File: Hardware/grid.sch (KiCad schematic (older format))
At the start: 269 parts, among them Q1 BSH205G2, Q10 BSH205G2, Q11 BSH205G2, Q12 BSH205G2, Q13 BSH205G2, Q14 BSH205G2, Q15 BSH205G2, Q16 BSH205G2, Q17 BSH205G2, Q18 BSH205G2, Q19 BSH205G2, Q2 BSH205G2, Q20 BSH205G2, Q21 NX7002AK, Q22 NX7002AK, Q23 NX7002AK, Q24 NX7002AK, Q25 NX7002AK, Q26 NX7002AK, Q27 NX7002AK, Q28 NX7002AK, Q29 NX7002AK, Q3 BSH205G2, Q30 NX7002AK, Q31 NX7002AK, Q32 NX7002AK, Q4 BSH205G2, Q5 BSH205G2, Q6 BSH205G2, Q7 BSH205G2, Q8 BSH205G2, Q9 BSH205G2, SW1 Button_matrix_4x4, SW10 SW_Push, SW11 SW_Push, SW12 SW_Push, SW13 SW_Push, SW14 SW_Push, SW15 SW_Push, SW16 SW_Push, SW17 SW_Push, SW18 SW_Push, SW19 SW_Push, SW2 Button_matrix_4x4, SW20 SW_Push, SW3 Button_matrix_4x4, SW4 Button_matrix_4x4, SW5 SW_Push, SW6 SW_Push, SW7 SW_Push, SW8 SW_Push, SW9 SW_Push, U2 74HC138, U3 74HC138, U4 74HC138

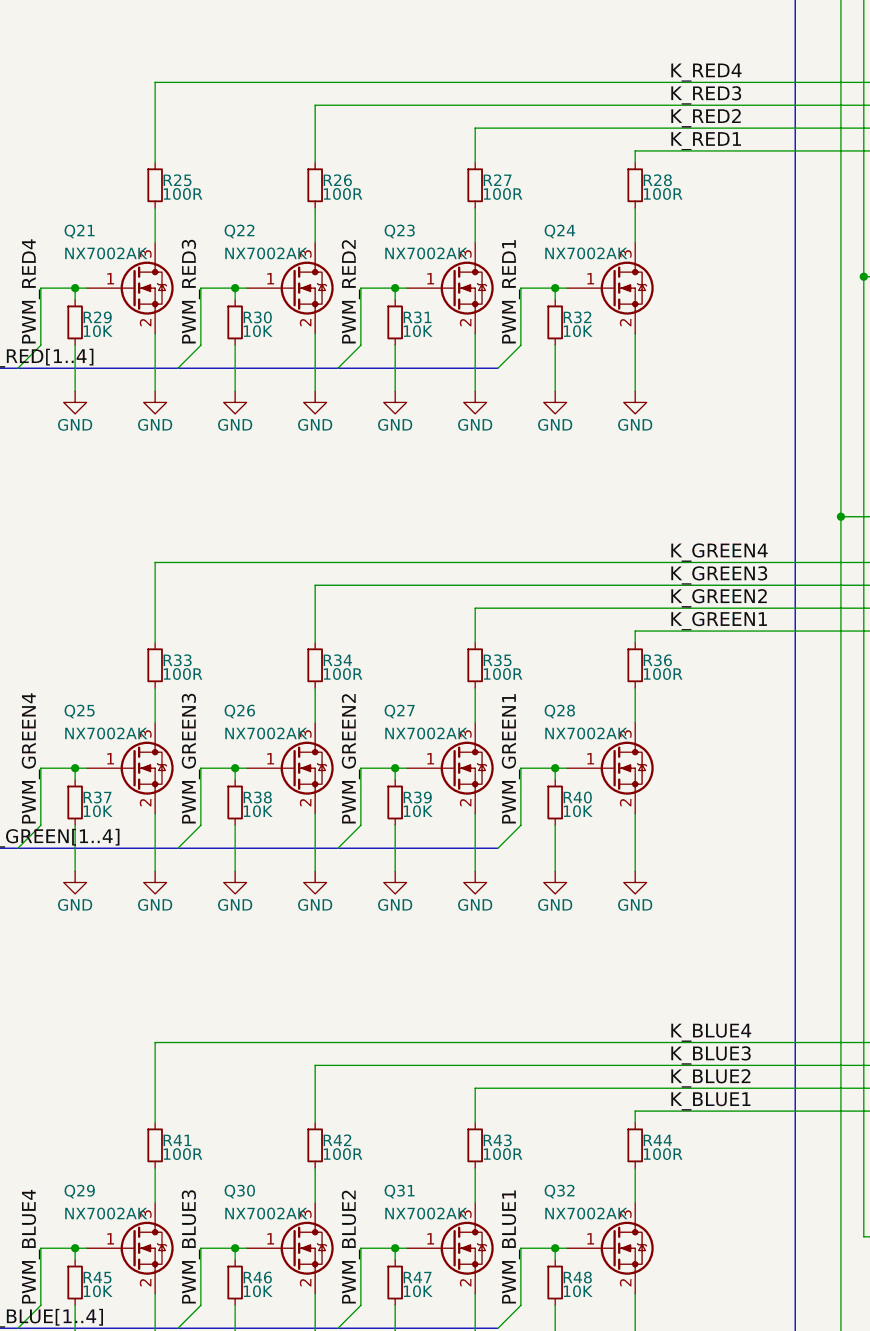
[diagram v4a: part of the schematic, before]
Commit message: changed LED current limiting resistor values
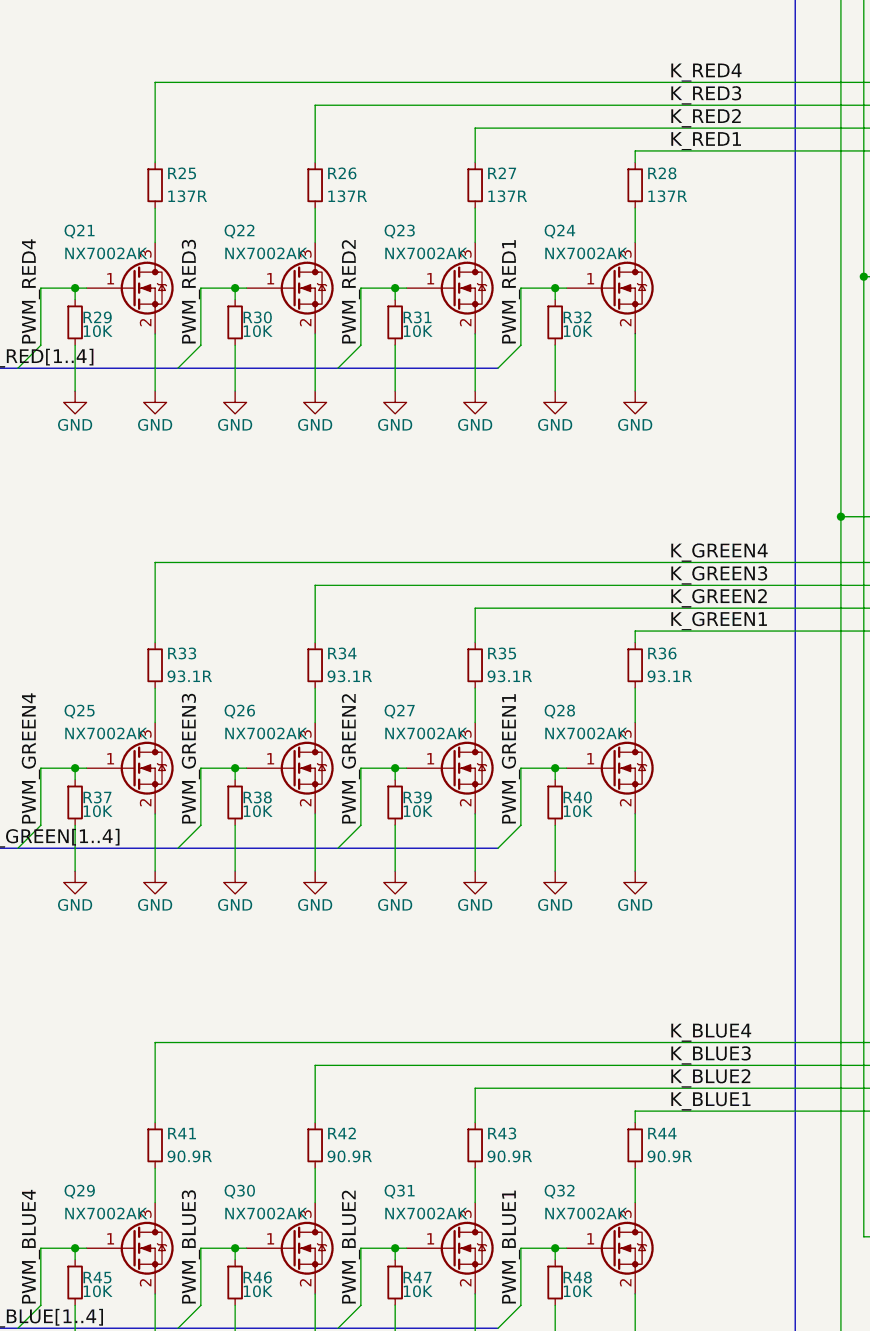
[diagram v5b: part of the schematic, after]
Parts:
- R25, R26, R27, R28: value 100R -> 137R
- R33, R34, R35, R36: value 100R -> 93.1R
- R41, R42, R43, R44: value 100R -> 90.9R
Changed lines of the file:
@@
 U 1 1 5A4E3C59
 P 4850 5800
-F 0 "R28" H 4880 5820 50  0000 L CNN
-F 1 "100R" H 4880 5760 50  0000 L CNN
+F 0 "R28" H 4900 5850 50  0000 L CNN
+F 1 "137R" H 4900 5750 50  0000 L CNN
 F 2 "project_library:R_1206" H 4850 5800 50  0001 C CNN
 F 3 "" H 4850 5800 50  0001 C CNN
@@
 U 1 1 5A4E72E9
 P 4150 5800
-F 0 "R27" H 4180 5820 50  0000 L CNN
-F 1 "100R" H 4180 5760 50  0000 L CNN
+F 0 "R27" H 4200 5850 50  0000 L CNN
+F 1 "137R" H 4200 5750 50  0000 L CNN
 F 2 "project_library:R_1206" H 4150 5800 50  0001 C CNN
 F 3 "" H 4150 5800 50  0001 C CNN
@@
 U 1 1 5A4E76B2
 P 3450 5800
-F 0 "R26" H 3480 5820 50  0000 L CNN
-F 1 "100R" H 3480 5760 50  0000 L CNN
+F 0 "R26" H 3500 5850 50  0000 L CNN
+F 1 "137R" H 3500 5750 50  0000 L CNN
 F 2 "project_library:R_1206" H 3450 5800 50  0001 C CNN
 F 3 "" H 3450 5800 50  0001 C CNN
@@
 U 1 1 5A4E7A7C
 P 2750 5800
-F 0 "R25" H 2780 5820 50  0000 L CNN
-F 1 "100R" H 2780 5760 50  0000 L CNN
+F 0 "R25" H 2800 5850 50  0000 L CNN
+F 1 "137R" H 2800 5750 50  0000 L CNN
 F 2 "project_library:R_1206" H 2750 5800 50  0001 C CNN
 F 3 "" H 2750 5800 50  0001 C CNN
@@
 U 1 1 5A4F1565
 P 4850 10000
-F 0 "R44" H 4880 10020 50  0000 L CNN
-F 1 "100R" H 4880 9960 50  0000 L CNN
+F 0 "R44" H 4900 10050 50  0000 L CNN
+F 1 "90.9R" H 4900 9950 50  0000 L CNN
 F 2 "project_library:R_1206" H 4850 10000 50  0001 C CNN
 F 3 "" H 4850 10000 50  0001 C CNN
@@
 U 1 1 5A4F156B
 P 4150 10000
-F 0 "R43" H 4180 10020 50  0000 L CNN
-F 1 "100R" H 4180 9960 50  0000 L CNN
+F 0 "R43" H 4200 10050 50  0000 L CNN
+F 1 "90.9R" H 4200 9950 50  0000 L CNN
 F 2 "project_library:R_1206" H 4150 10000 50  0001 C CNN
 F 3 "" H 4150 10000 50  0001 C CNN
@@
 U 1 1 5A4F1571
 P 3450 10000
-F 0 "R42" H 3480 10020 50  0000 L CNN
-F 1 "100R" H 3480 9960 50  0000 L CNN
+F 0 "R42" H 3500 10050 50  0000 L CNN
+F 1 "90.9R" H 3500 9950 50  0000 L CNN
 F 2 "project_library:R_1206" H 3450 10000 50  0001 C CNN
 F 3 "" H 3450 10000 50  0001 C CNN
@@
 U 1 1 5A4F1577
 P 2750 10000
-F 0 "R41" H 2780 10020 50  0000 L CNN
-F 1 "100R" H 2780 9960 50  0000 L CNN
+F 0 "R41" H 2800 10050 50  0000 L CNN
+F 1 "90.9R" H 2800 9950 50  0000 L CNN
 F 2 "project_library:R_1206" H 2750 10000 50  0001 C CNN
 F 3 "" H 2750 10000 50  0001 C CNN
@@
 U 1 1 5A4FC77F
 P 4850 7900
-F 0 "R36" H 4880 7920 50  0000 L CNN
-F 1 "100R" H 4880 7860 50  0000 L CNN
+F 0 "R36" H 4900 7950 50  0000 L CNN
+F 1 "93.1R" H 4900 7850 50  0000 L CNN
 F 2 "project_library:R_1206" H 4850 7900 50  0001 C CNN
 F 3 "" H 4850 7900 50  0001 C CNN
@@
 U 1 1 5A4FC785
 P 4150 7900
-F 0 "R35" H 4180 7920 50  0000 L CNN
-F 1 "100R" H 4180 7860 50  0000 L CNN
+F 0 "R35" H 4200 7950 50  0000 L CNN
+F 1 "93.1R" H 4200 7850 50  0000 L CNN
 F 2 "project_library:R_1206" H 4150 7900 50  0001 C CNN
 F 3 "" H 4150 7900 50  0001 C CNN
@@
 U 1 1 5A4FC78B
 P 3450 7900
-F 0 "R34" H 3480 7920 50  0000 L CNN
-F 1 "100R" H 3480 7860 50  0000 L CNN
+F 0 "R34" H 3500 7950 50  0000 L CNN
+F 1 "93.1R" H 3500 7850 50  0000 L CNN
 F 2 "project_library:R_1206" H 3450 7900 50  0001 C CNN
 F 3 "" H 3450 7900 50  0001 C CNN
@@
 U 1 1 5A4FC791
 P 2750 7900
-F 0 "R33" H 2780 7920 50  0000 L CNN
-F 1 "100R" H 2780 7860 50  0000 L CNN
+F 0 "R33" H 2800 7950 50  0000 L CNN
+F 1 "93.1R" H 2800 7850 50  0000 L CNN
 F 2 "project_library:R_1206" H 2750 7900 50  0001 C CNN
 F 3 "" H 2750 7900 50  0001 C CNN

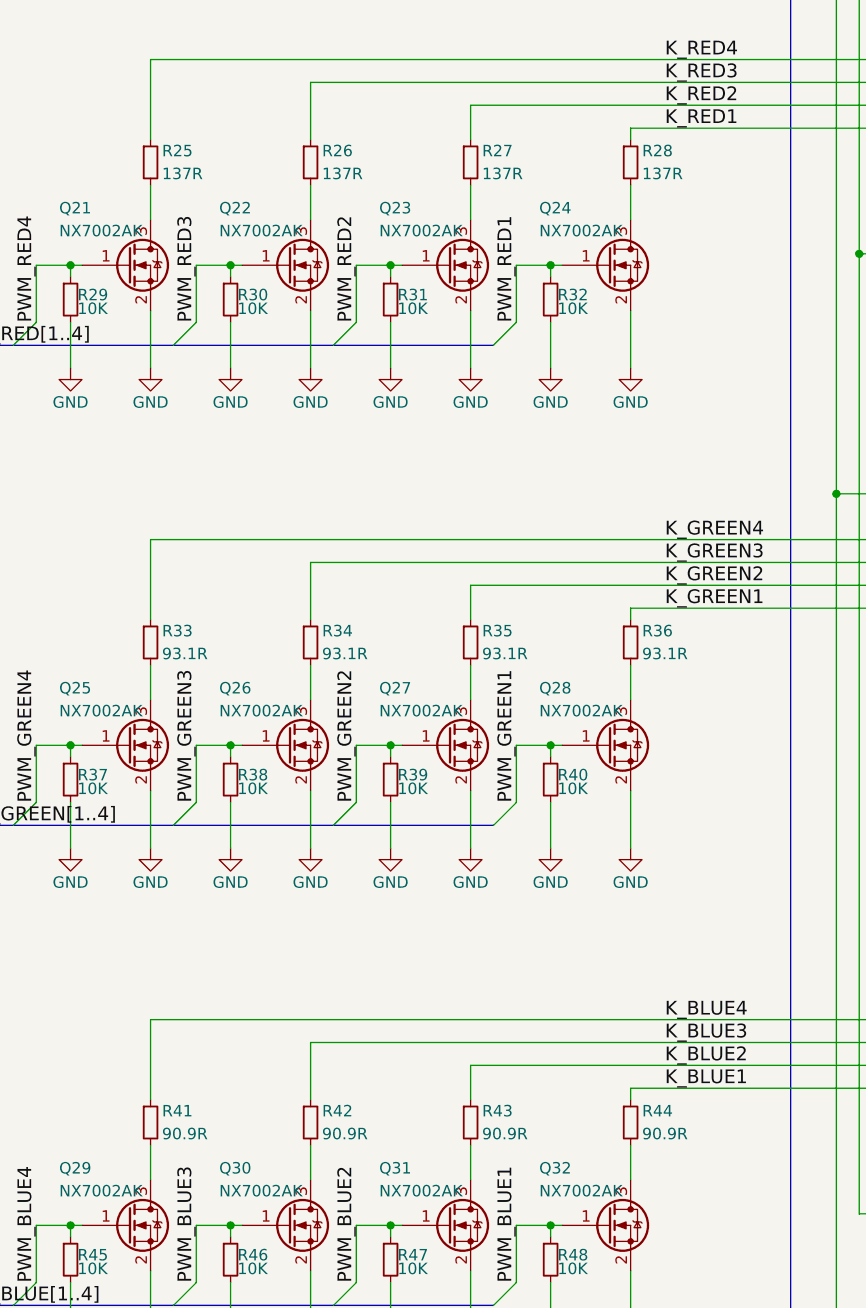
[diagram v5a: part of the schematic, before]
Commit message: changed resistor values, added drum layout output
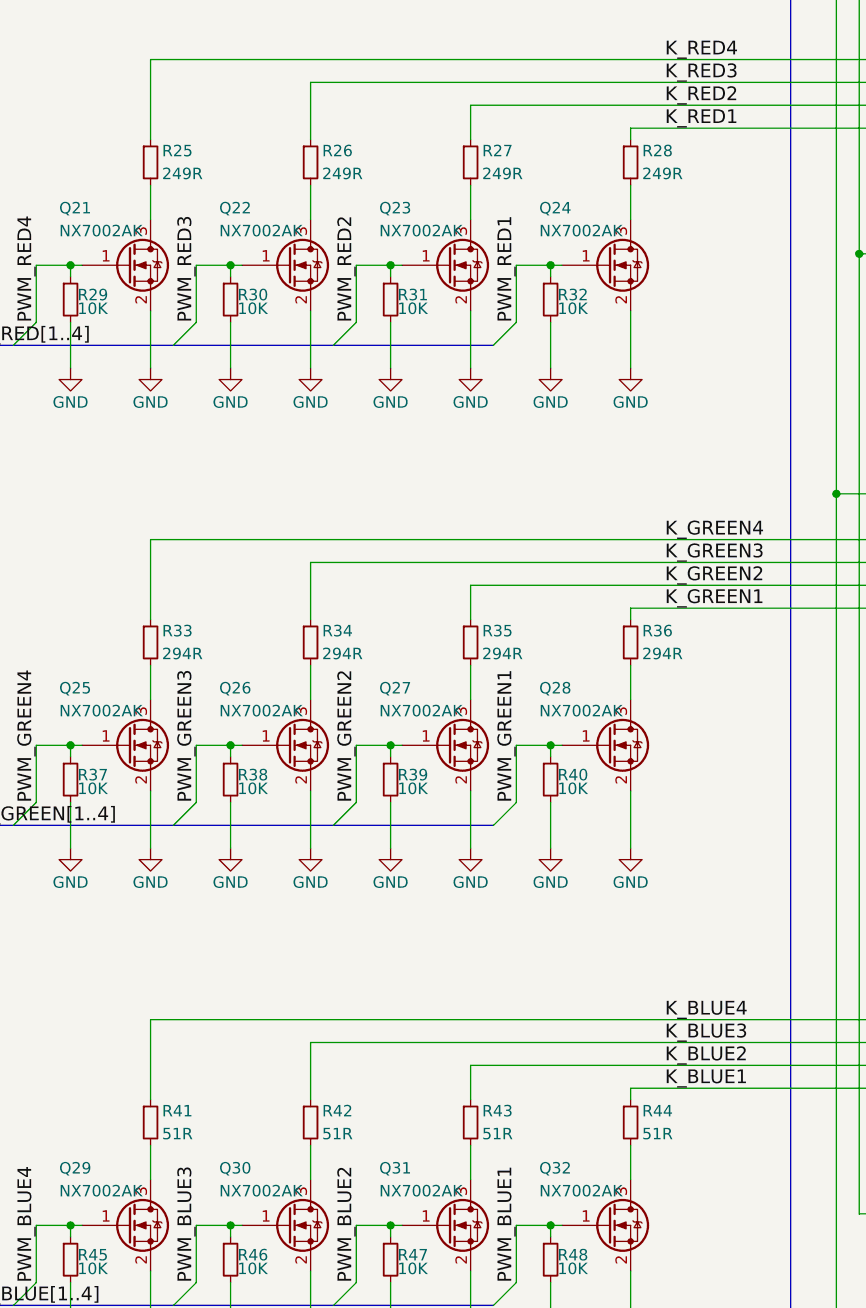
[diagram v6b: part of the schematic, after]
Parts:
- R25, R26, R27, R28: value 137R -> 249R
- R33, R34, R35, R36: value 93.1R -> 294R
- R41, R42, R43, R44: value 90.9R -> 51R
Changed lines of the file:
@@
 P 4850 5800
 F 0 "R28" H 4900 5850 50  0000 L CNN
-F 1 "137R" H 4900 5750 50  0000 L CNN
+F 1 "249R" H 4900 5750 50  0000 L CNN
 F 2 "project_library:R_1206" H 4850 5800 50  0001 C CNN
 F 3 "" H 4850 5800 50  0001 C CNN
@@
 P 4150 5800
 F 0 "R27" H 4200 5850 50  0000 L CNN
-F 1 "137R" H 4200 5750 50  0000 L CNN
+F 1 "249R" H 4200 5750 50  0000 L CNN
 F 2 "project_library:R_1206" H 4150 5800 50  0001 C CNN
 F 3 "" H 4150 5800 50  0001 C CNN
@@
 P 3450 5800
 F 0 "R26" H 3500 5850 50  0000 L CNN
-F 1 "137R" H 3500 5750 50  0000 L CNN
+F 1 "249R" H 3500 5750 50  0000 L CNN
 F 2 "project_library:R_1206" H 3450 5800 50  0001 C CNN
 F 3 "" H 3450 5800 50  0001 C CNN
@@
 P 2750 5800
 F 0 "R25" H 2800 5850 50  0000 L CNN
-F 1 "137R" H 2800 5750 50  0000 L CNN
+F 1 "249R" H 2800 5750 50  0000 L CNN
 F 2 "project_library:R_1206" H 2750 5800 50  0001 C CNN
 F 3 "" H 2750 5800 50  0001 C CNN
@@
 P 4850 10000
 F 0 "R44" H 4900 10050 50  0000 L CNN
-F 1 "90.9R" H 4900 9950 50  0000 L CNN
+F 1 "51R" H 4900 9950 50  0000 L CNN
 F 2 "project_library:R_1206" H 4850 10000 50  0001 C CNN
 F 3 "" H 4850 10000 50  0001 C CNN
@@
 P 4150 10000
 F 0 "R43" H 4200 10050 50  0000 L CNN
-F 1 "90.9R" H 4200 9950 50  0000 L CNN
+F 1 "51R" H 4200 9950 50  0000 L CNN
 F 2 "project_library:R_1206" H 4150 10000 50  0001 C CNN
 F 3 "" H 4150 10000 50  0001 C CNN
@@
 P 3450 10000
 F 0 "R42" H 3500 10050 50  0000 L CNN
-F 1 "90.9R" H 3500 9950 50  0000 L CNN
+F 1 "51R" H 3500 9950 50  0000 L CNN
 F 2 "project_library:R_1206" H 3450 10000 50  0001 C CNN
 F 3 "" H 3450 10000 50  0001 C CNN
@@
 P 2750 10000
 F 0 "R41" H 2800 10050 50  0000 L CNN
-F 1 "90.9R" H 2800 9950 50  0000 L CNN
+F 1 "51R" H 2800 9950 50  0000 L CNN
 F 2 "project_library:R_1206" H 2750 10000 50  0001 C CNN
 F 3 "" H 2750 10000 50  0001 C CNN
@@
 P 4850 7900
 F 0 "R36" H 4900 7950 50  0000 L CNN
-F 1 "93.1R" H 4900 7850 50  0000 L CNN
+F 1 "294R" H 4900 7850 50  0000 L CNN
 F 2 "project_library:R_1206" H 4850 7900 50  0001 C CNN
 F 3 "" H 4850 7900 50  0001 C CNN
@@
 P 4150 7900
 F 0 "R35" H 4200 7950 50  0000 L CNN
-F 1 "93.1R" H 4200 7850 50  0000 L CNN
+F 1 "294R" H 4200 7850 50  0000 L CNN
 F 2 "project_library:R_1206" H 4150 7900 50  0001 C CNN
 F 3 "" H 4150 7900 50  0001 C CNN
@@
 P 3450 7900
 F 0 "R34" H 3500 7950 50  0000 L CNN
-F 1 "93.1R" H 3500 7850 50  0000 L CNN
+F 1 "294R" H 3500 7850 50  0000 L CNN
 F 2 "project_library:R_1206" H 3450 7900 50  0001 C CNN
 F 3 "" H 3450 7900 50  0001 C CNN
@@
 P 2750 7900
 F 0 "R33" H 2800 7950 50  0000 L CNN
-F 1 "93.1R" H 2800 7850 50  0000 L CNN
+F 1 "294R" H 2800 7850 50  0000 L CNN
 F 2 "project_library:R_1206" H 2750 7900 50  0001 C CNN
 F 3 "" H 2750 7900 50  0001 C CNN

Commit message: converted all components except big tactile switches
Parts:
- C1, C2, C3: symbol C_Small -> project_library:C_Small
- D1, D101, D103, D105, D107, D109, D11, D111, D113, D115, D117, D119, D121, D123, D125, D127, D129, D13, D132, D134, D136, D140, D142, D144, D146, D148, D15, D150, D152, D154, D156, D17, D19, D21, D23, D25, D27, D29, D3, D31, D33, D35, D37, D39, D41, D43, D45, D47, D49, D5, D51, D53, D55, D57, D59, D61, D63, D65, D67, D69, D7, D71, D73, D75, D77, D79, D81, D83, D85, D87, D89, D9, D91, D93, D95, D97, D99: symbol LED_RAGB -> project_library:LED_RAGB
- D10, D100, D102, D104, D106, D108, D110, D112, D114, D116, D118, D12, D120, D122, D124, D126, D128, D130, D131, D133, D135, D137, D138, D139, D14, D141, D143, D145, D147, D149, D151, D153, D155, D157, D16, D18, D2, D20, D22, D24, D26, D28, D30, D32, D34, D36, D38, D4, D40, D42, D44, D46, D48, D50, D52, D54, D56, D58, D6, D60, D62, D64, D66, D68, D70, D72, D74, D76, D78, D8, D80, D82, D84, D86, D88, D90, D92, D94, D96, D98: symbol LL4148 -> project_library:LL4148
- Q1, Q10, Q11, Q12, Q13, Q14, Q15, Q16, Q17, Q18, Q19, Q2, Q20, Q3, Q4, Q5, Q6, Q7, Q8, Q9: symbol BSS83P -> project_library:BSS83P
- Q21, Q22, Q23, Q24, Q25, Q26, Q27, Q28, Q29, Q30, Q31, Q32: symbol 2N7002 -> project_library:2N7002
- R1, R10, R11, R12, R13, R14, R15, R16, R17, R18, R19, R2, R20, R21, R22, R23, R24, R25, R26, R27, R28, R29, R3, R30, R31, R32, R33, R34, R35, R36, R37, R38, R39, R4, R40, R41, R42, R43, R44, R45, R46, R47, R48, R49, R5, R50, R51, R52, R53, R54, R6, R7, R8, R9: symbol R_Small -> project_library:R_Small
- SW1, SW2, SW3, SW4: symbol Button_matrix_4x4 -> project_library:Button_matrix_4x4
- SW10, SW11, SW12, SW13, SW14, SW15, SW16, SW17, SW18, SW19, SW20, SW5, SW6, SW7, SW8, SW9: symbol SW_Push -> project_library:SW_Push
- U2, U3, U4: symbol 74LS138 -> project_library:74LS138

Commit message: replaced all models with .step, deleted .wrl models
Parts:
- SW10, SW12, SW13, SW14, SW15, SW16, SW17, SW18, SW19, SW20, SW5, SW7: footprint project_library:Tactile_switch_12x12_black_cap -> project_library:Tactile_switch_12x12
- SW11, SW6, SW8, SW9: footprint project_library:Tactile_switch_12x12_black_cap_no_holes -> project_library:Tactile_switch_12x12_no_holes
